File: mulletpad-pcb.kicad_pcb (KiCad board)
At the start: 2 copper layers, 73.4 x 98.1 mm, 56 parts, among them SW0 KEYSW, SW1 KEYSW, SW10 KEYSW, SW11 KEYSW, SW12 KEYSW, SW13 KEYSW, SW14 KEYSW, SW15 KEYSW, SW16 KEYSW, SW2 KEYSW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

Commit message: update ground fills for usb port and xtal
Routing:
- net row0: track 158.7 -> 159.3 mm
- added copper zone on B.Cu, net GND
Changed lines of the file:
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@@
     (thickness 1.6)
     (drawings 540)
-    (tracks 593)
+    (tracks 595)
     (zones 0)
     (modules 56)
@@
   (segment (start 108.933999 73.238759) (end 110.287793 74.592553) (width 0.25) (layer B.Cu) (net 6))
   (segment (start 110.287793 74.592553) (end 110.392779 74.697539) (width 0.25) (layer B.Cu) (net 6))
-  (segment (start 177.72894 48.511366) (end 178.128939 48.111367) (width 0.25) (layer F.Cu) (net 6))
   (via (at 178.128939 48.111367) (size 0.8) (drill 0.4) (layers F.Cu B.Cu) (net 6))
-  (segment (start 175.85155 50.388756) (end 177.72894 48.511366) (width 0.25) (layer F.Cu) (net 6))
   (segment (start 178.106493 48.133813) (end 178.128939 48.111367) (width 0.25) (layer B.Cu) (net 6))
   (segment (start 178.106493 49.708493) (end 178.106493 48.133813) (width 0.25) (layer B.Cu) (net 6))
-  (segment (start 175.85155 53.595353) (end 175.85155 50.388756) (width 0.25) (layer F.Cu) (net 6))
-  (segment (start 170.392278 59.054625) (end 175.85155 53.595353) (width 0.25) (layer F.Cu) (net 6))
-  (segment (start 151.862249 59.054625) (end 170.392278 59.054625) (width 0.25) (layer F.Cu) (net 6))
   (segment (start 172.964435 67.128995) (end 172.964435 67.974839) (width 0.25) (layer B.Cu) (net 6))
   (segment (start 169.657376 69.395746) (end 166.822754 72.230368) (width 0.25) (layer B.Cu) (net 6))
@@
   (segment (start 110.617274 74.922034) (end 110.287793 74.592553) (width 0.25) (layer B.Cu) (net 6))
   (segment (start 171.543528 69.395746) (end 169.657376 69.395746) (width 0.25) (layer B.Cu) (net 6))
+  (segment (start 177.72894 48.511366) (end 178.128939 48.111367) (width 0.25) (layer F.Cu) (net 6))
+  (segment (start 151.862249 59.054625) (end 166.297824 59.054625) (width 0.25) (layer F.Cu) (net 6))
+  (segment (start 168.922474 56.429975) (end 168.922474 52.172524) (width 0.25) (layer F.Cu) (net 6))
+  (segment (start 166.297824 59.054625) (end 168.922474 56.429975) (width 0.25) (layer F.Cu) (net 6))
+  (segment (start 168.922474 52.172524) (end 172.552997 48.542001) (width 0.25) (layer F.Cu) (net 6))
+  (segment (start 172.552997 48.542001) (end 177.698305 48.542001) (width 0.25) (layer F.Cu) (net 6))
+  (segment (start 177.698305 48.542001) (end 177.72894 48.511366) (width 0.25) (layer F.Cu) (net 6))
   (segment (start 111.379 55.1195) (end 112.066 55.8065) (width 0.25) (layer B.Cu) (net 7))
   (segment (start 111.379 49.657) (end 111.379 55.1195) (width 0.25) (layer B.Cu) (net 7))
@@
   (segment (start 168.989435 64.778995) (end 169.614435 64.778995) (width 0.25) (layer B.Cu) (net 59))
   (segment (start 163.459341 64.778995) (end 168.989435 64.778995) (width 0.25) (layer B.Cu) (net 59))
+  (zone (net 2) (net_name GND) (layer B.Cu) (hatch edge 0.508)
+    (connect_pads (clearance 0.508))
+    (min_thickness 0.254)
+    (fill yes (arc_segments 16) (thermal_gap 0.508) (thermal_bridge_width 0.508))
+    (polygon
+      (pts
+        (xy 156.901577 38.477369) (xy 156.849084 44.199106) (xy 166.560289 44.356585) (xy 166.560289 38.424876)
+      )
+    )
+  )
+  (zone (net 2) (net_name GND) (layer B.Cu) (hatch edge 0.508)
+    (connect_pads (clearance 0.508))
+    (min_thickness 0.254)
+    (fill yes (arc_segments 16) (thermal_gap 0.508) (thermal_bridge_width 0.508))
+    (polygon
+      (pts
+        (xy 180.470934 58.949639) (xy 178.528693 58.975886) (xy 177.531326 58.897146) (xy 177.478833 59.422076) (xy 177.301669 61.101852)
+        (xy 173.909309 61.101852) (xy 170.808627 58.162244) (xy 169.867348 58.162244) (xy 169.867348 53.490367) (xy 180.365948 53.490367)
+      )
+    )
+  )
 )

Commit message: Update gnd fills for xtal
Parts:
- R6: value 22 -> 22Ω

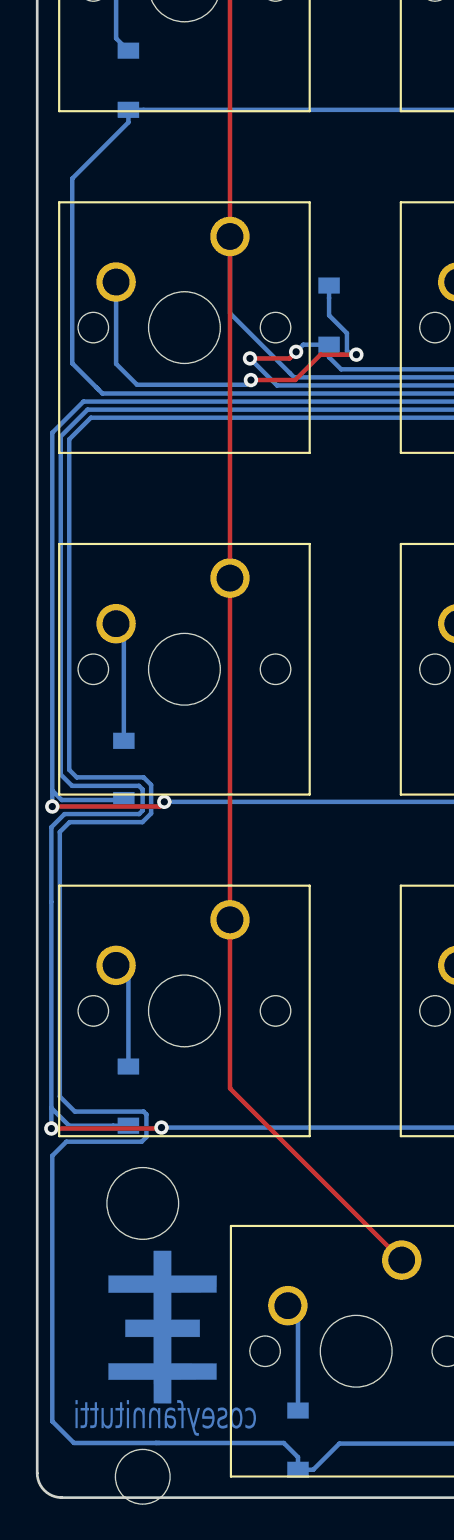
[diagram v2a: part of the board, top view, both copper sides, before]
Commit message: update component labels
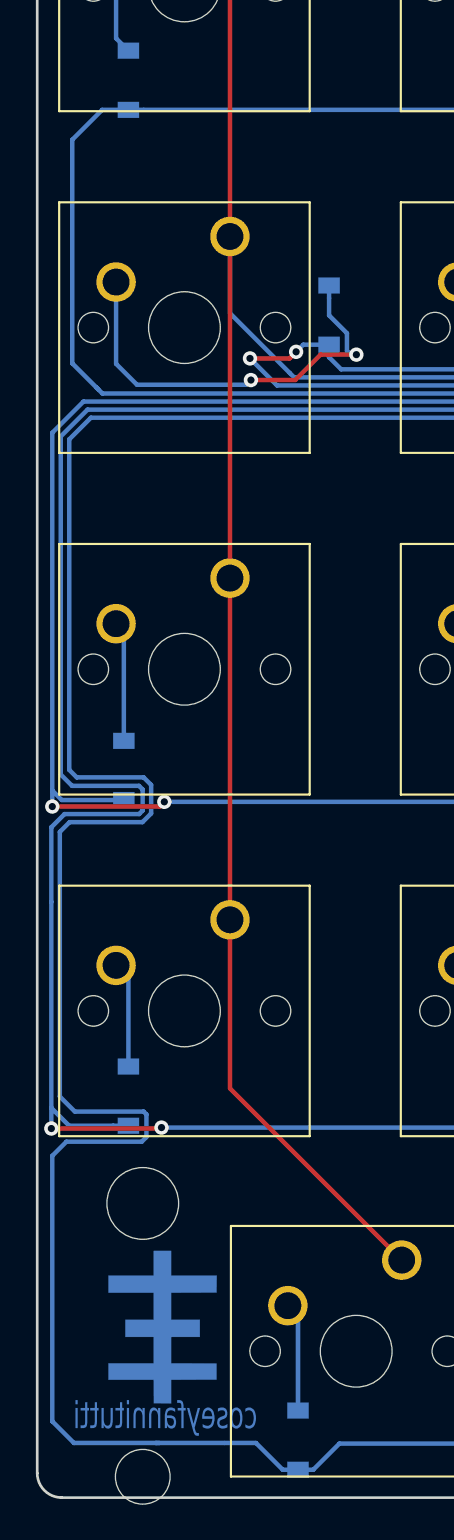
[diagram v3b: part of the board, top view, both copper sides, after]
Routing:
- net row0: track 159.3 -> 160.2 mm
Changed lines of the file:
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@@
     (thickness 1.6)
     (drawings 540)
-    (tracks 595)
+    (tracks 596)
     (zones 0)
     (modules 56)
@@
   (segment (start 151.810374 59.1065) (end 151.862249 59.054625) (width 0.25) (layer B.Cu) (net 6))
   (segment (start 177.533704 49.708493) (end 178.106493 49.708493) (width 0.25) (layer B.Cu) (net 6))
-  (segment (start 108.933999 62.938501) (end 108.933999 73.238759) (width 0.25) (layer B.Cu) (net 6))
-  (segment (start 112.066 59.8065) (end 108.933999 62.938501) (width 0.25) (layer B.Cu) (net 6))
-  (segment (start 112.066 59.1065) (end 112.066 59.8065) (width 0.25) (layer B.Cu) (net 6))
-  (segment (start 108.933999 73.238759) (end 110.287793 74.592553) (width 0.25) (layer B.Cu) (net 6))
   (segment (start 110.287793 74.592553) (end 110.392779 74.697539) (width 0.25) (layer B.Cu) (net 6))
   (via (at 178.128939 48.111367) (size 0.8) (drill 0.4) (layers F.Cu B.Cu) (net 6))
@@
   (segment (start 172.552997 48.542001) (end 177.698305 48.542001) (width 0.25) (layer F.Cu) (net 6))
   (segment (start 177.698305 48.542001) (end 177.72894 48.511366) (width 0.25) (layer F.Cu) (net 6))
+  (segment (start 110.602751 59.1065) (end 112.066 59.1065) (width 0.25) (layer B.Cu) (net 6))
+  (segment (start 108.933999 60.775252) (end 110.602751 59.1065) (width 0.25) (layer B.Cu) (net 6))
+  (segment (start 108.933999 73.238759) (end 108.933999 60.775252) (width 0.25) (layer B.Cu) (net 6))
+  (segment (start 110.287793 74.592553) (end 108.933999 73.238759) (width 0.25) (layer B.Cu) (net 6))
   (segment (start 111.379 55.1195) (end 112.066 55.8065) (width 0.25) (layer B.Cu) (net 7))
   (segment (start 111.379 49.657) (end 111.379 55.1195) (width 0.25) (layer B.Cu) (net 7))
@@
   (segment (start 108.293059 96.167176) (end 108.922975 96.797092) (width 0.25) (layer B.Cu) (net 13))
   (segment (start 108.922975 96.797092) (end 112.655594 96.797092) (width 0.25) (layer B.Cu) (net 13))
-  (segment (start 120.728774 133.437206) (end 113.594852 133.437206) (width 0.25) (layer B.Cu) (net 14))
-  (segment (start 121.521295 134.229727) (end 120.728774 133.437206) (width 0.25) (layer B.Cu) (net 14))
-  (segment (start 121.521295 134.929727) (end 121.521295 134.229727) (width 0.25) (layer B.Cu) (net 14))
   (segment (start 113.594852 133.437206) (end 113.804824 133.437206) (width 0.25) (layer B.Cu) (net 14))
   (segment (start 149.062 134.798) (end 149.912 134.798) (width 0.25) (layer B.Cu) (net 14))
@@
   (segment (start 113.332387 98.339526) (end 112.85002 98.821892) (width 0.25) (layer B.Cu) (net 14))
   (segment (start 112.85002 98.821892) (end 108.787923 98.821892) (width 0.25) (layer B.Cu) (net 14))
+  (segment (start 119.178774 133.437206) (end 117.426841 133.437206) (width 0.25) (layer B.Cu) (net 14))
+  (segment (start 120.671295 134.929727) (end 119.178774 133.437206) (width 0.25) (layer B.Cu) (net 14))
+  (segment (start 121.521295 134.929727) (end 120.671295 134.929727) (width 0.25) (layer B.Cu) (net 14))
+  (segment (start 117.426841 133.437206) (end 113.594852 133.437206) (width 0.25) (layer B.Cu) (net 14))
   (segment (start 121.521295 126.347295) (end 120.956 125.782) (width 0.25) (layer B.Cu) (net 15))
   (segment (start 121.521295 131.629727) (end 121.521295 126.347295) (width 0.25) (layer B.Cu) (net 15))
